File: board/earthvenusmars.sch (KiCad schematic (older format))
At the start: 33 parts, among them J1 Conn_01x05_Female, SW1 SW_SPST, SW2 SW_SPST, U1 ATSAMD21G18A-AU, U2 MIC5504-3.3YM5, Y1 32768Hz

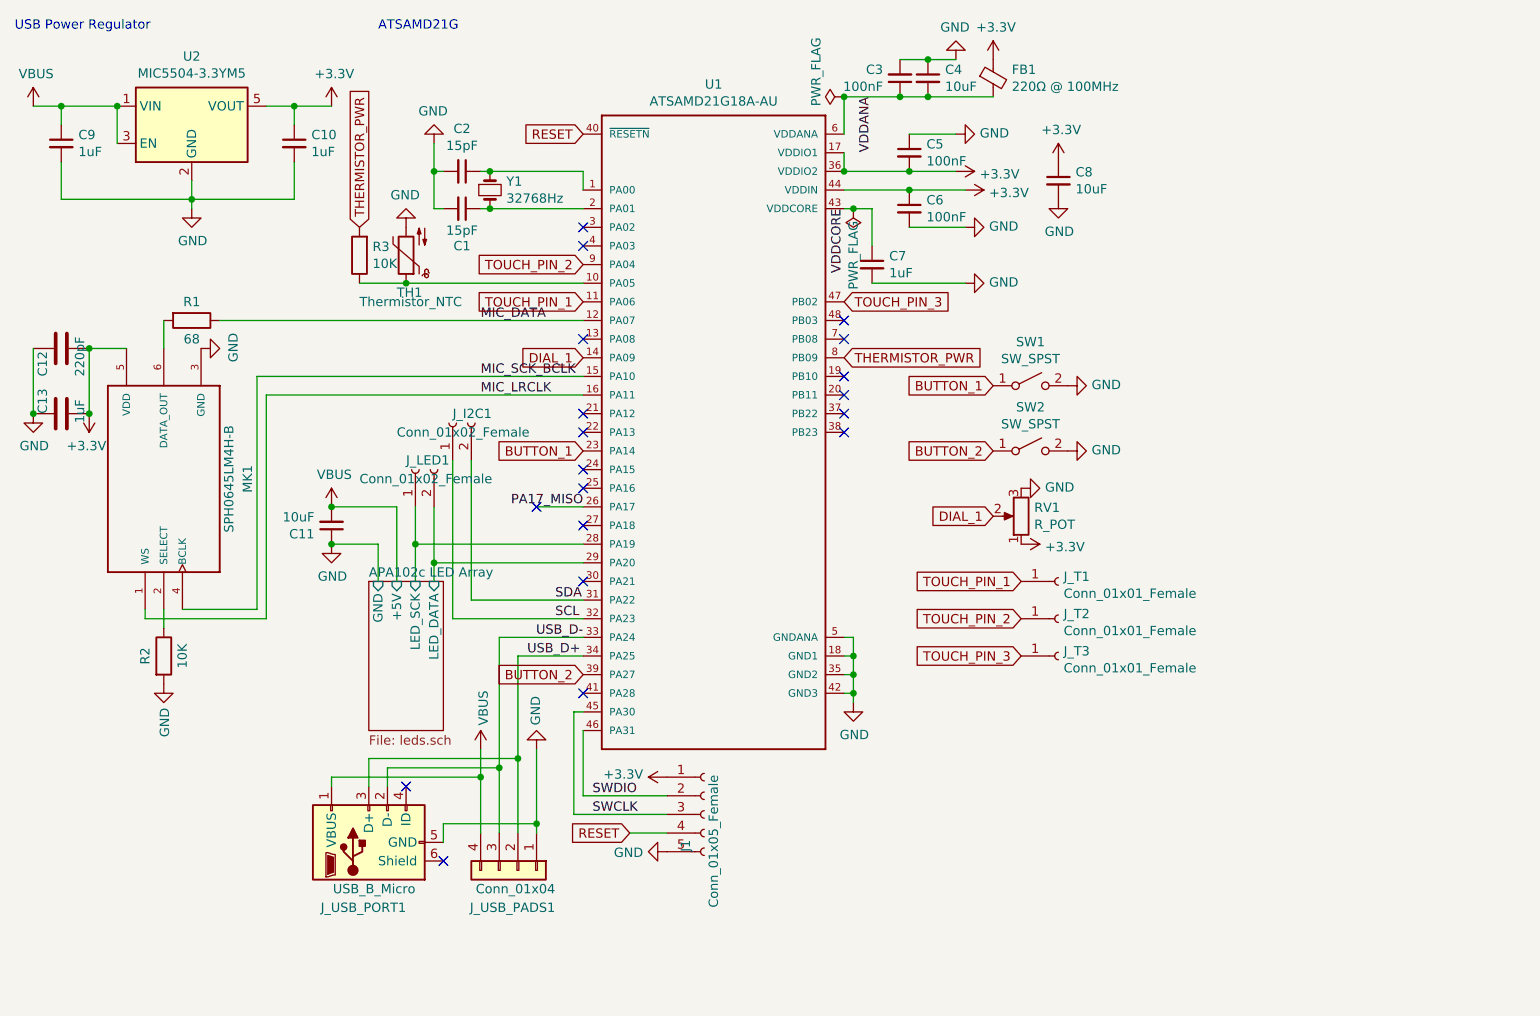
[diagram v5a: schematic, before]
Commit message: add a power switch. ugh. but it's going to prevent the device from waking up in a backpack and stuff; not to mention power draw is way too high for sleep right now
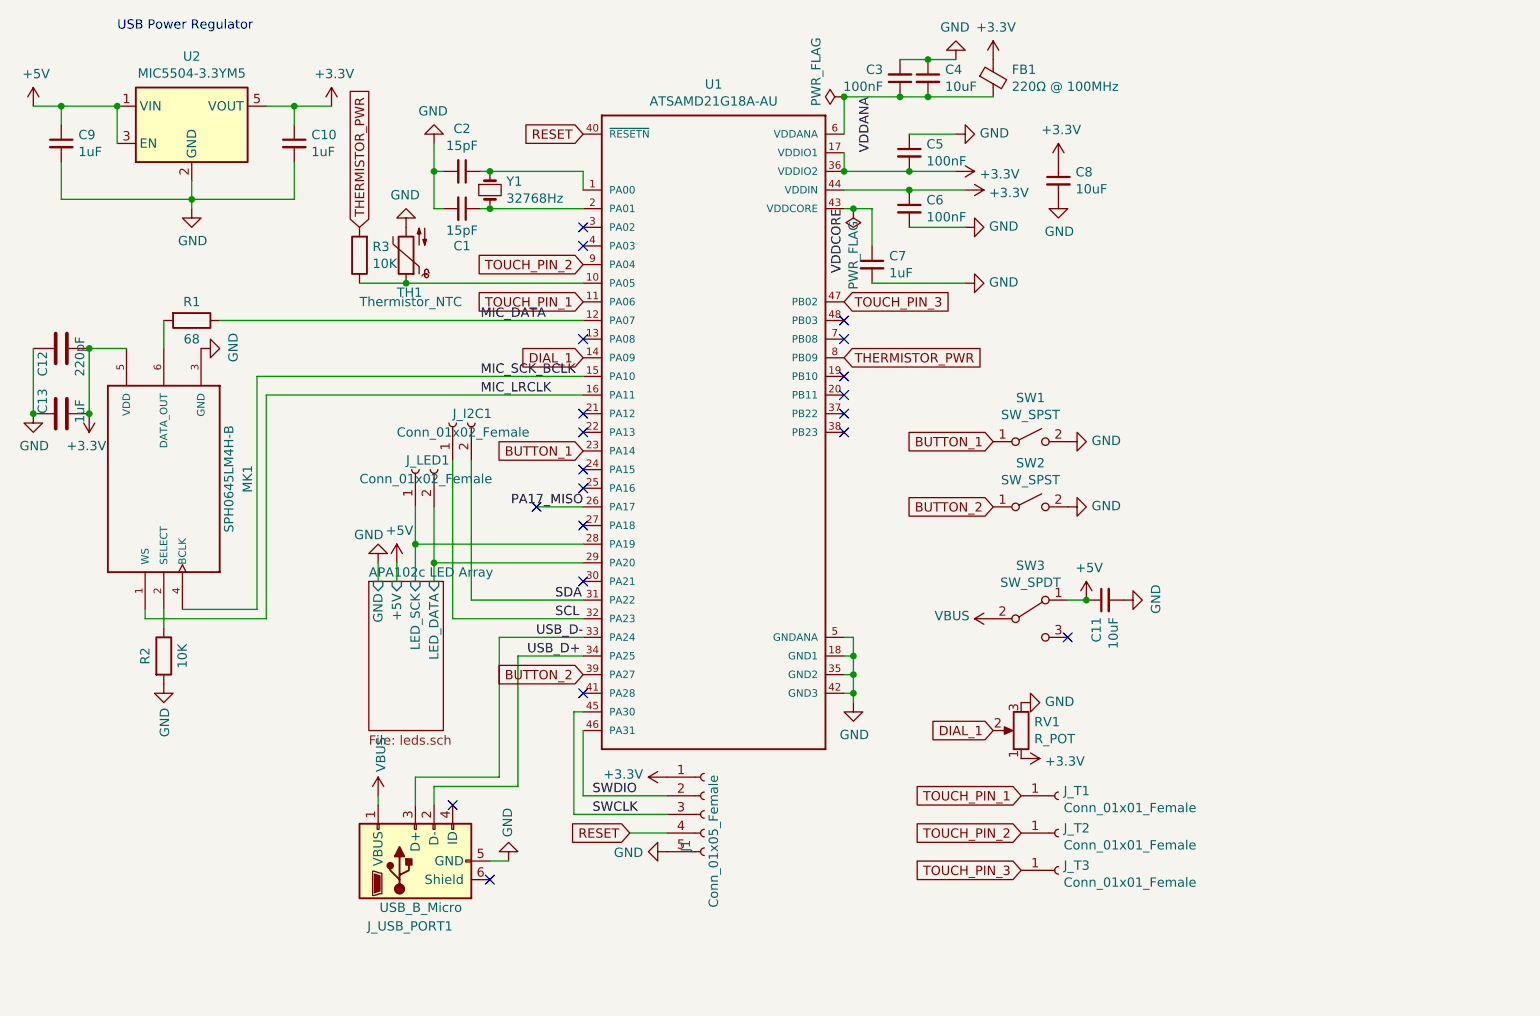
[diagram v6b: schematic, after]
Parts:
- removed J_USB_PADS1: Conn_01x04, earthvenusmars:USB_SMD, symbol Connector_Generic:Conn_01x04
- added SW3: SW_SPDT, earthvenusmars:COPAL-MFS101D-6-Z, symbol Switch:SW_SPDT
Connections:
- net GND: now also C11.2; no longer C11.1
- net USB_D+: now also J_USB_PORT1.2 (D-); no longer J_USB_PORT1.3 (D+)
- net USB_D-: now also J_USB_PORT1.3 (D+); no longer J_USB_PORT1.2 (D-)
- net VBUS: now also SW3.2 (B); no longer C11.2, C9.1, U2.1 (VIN), U2.3 (EN)
- new net +5V: C11.1, C9.1, SW3.1 (A), U2.1 (VIN), U2.3 (EN)
- no-connect marks 19 -> 20
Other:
- note removed: "ATSAMD21G"
- moved on the sheet: C11, J_T1, J_T2, J_T3, J_USB_PORT1, RV1, SW1, SW2

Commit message: clean up schematic a bit; reroute +5v to save a via
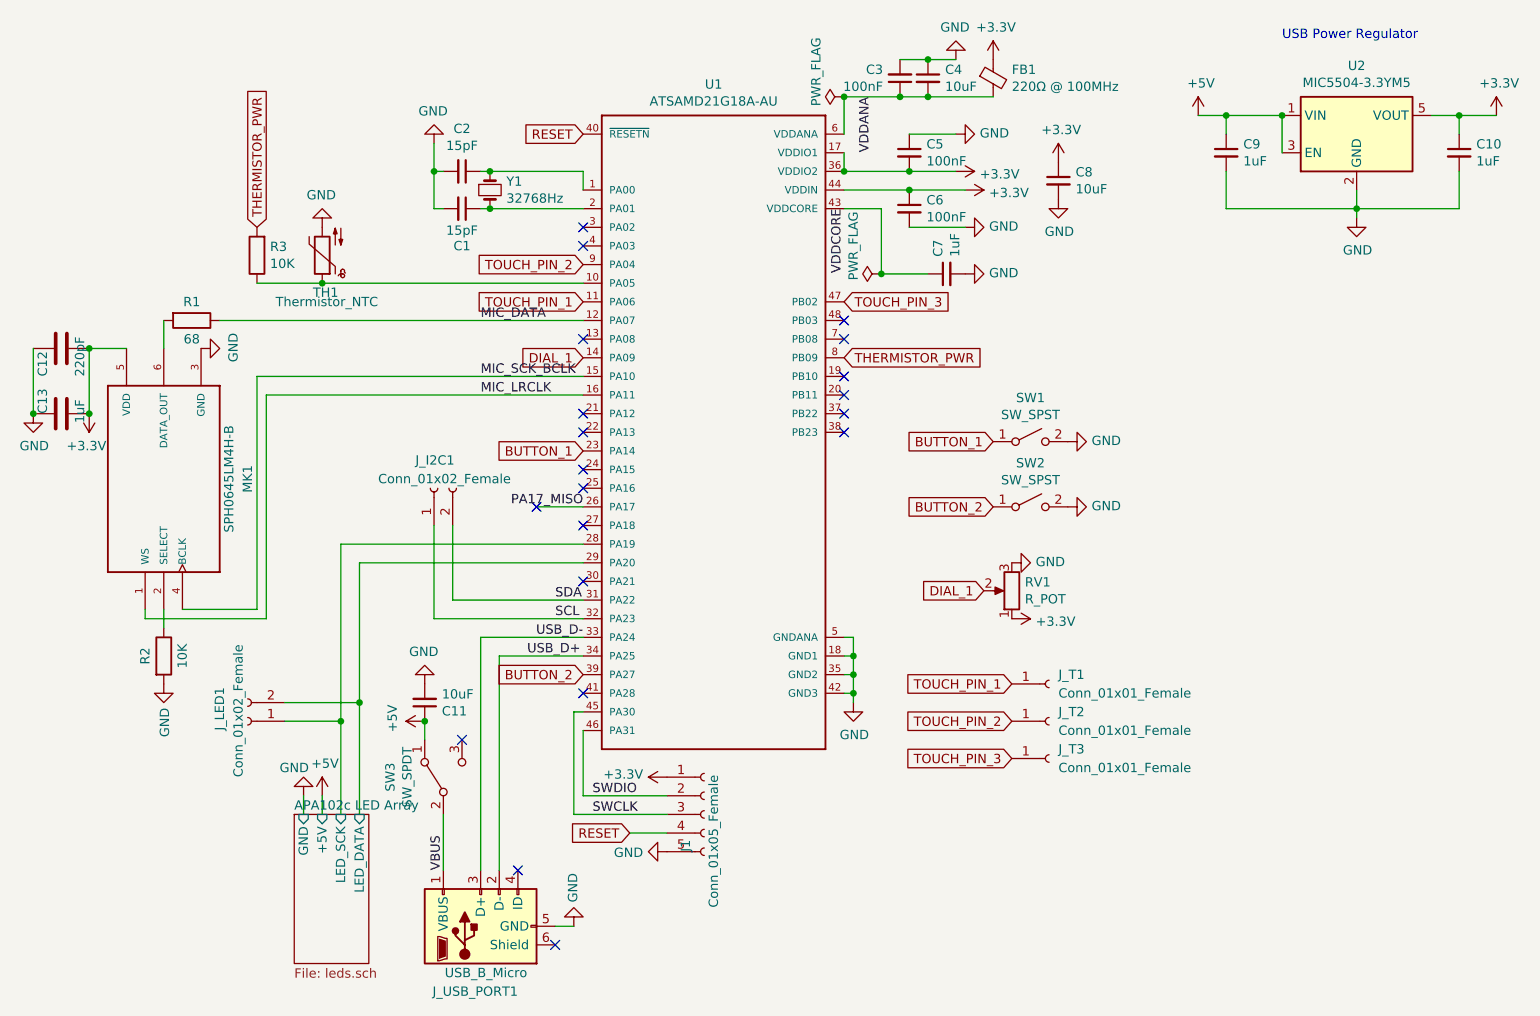
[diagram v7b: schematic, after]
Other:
- moved on the sheet: C10, C11, C7, C9, J_I2C1, J_LED1, J_T1, J_T2, J_T3, J_USB_PORT1, R3, RV1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

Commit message: add some part numbers to designation fields because fab often doesn't find the parts in other fields
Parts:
- J_USB_PORT1: Designation (none) -> USB3076-30-A
- RV1: Designation (none) -> 3352T-1-103LF
- SW3: Designation (none) -> COPAL-MFS101D-6-Z
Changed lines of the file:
@@
 F 2 "Pot_dial_3352T-1-103LF:Pot_dial_3352T-1-103LF" H 6250 3800 50  0001 C CNN
 F 3 "~" H 6250 3800 50  0001 C CNN
+F 4 "3352T-1-103LF" H 6250 3800 50  0001 C CNN "Designation"
 	1    6250 3800
 	-1   0    0    1
@@
 F 2 "earthvenusmars:COPAL-MFS101D-6-Z" H 3200 4800 50  0001 C CNN
 F 3 "~" H 3200 4800 50  0001 C CNN
+F 4 "COPAL-MFS101D-6-Z" H 3200 4800 50  0001 C CNN "Designation"
 	1    3200 4800
 	0    -1   -1   0
@@
 F 2 "Connector_USB:USB_Micro-B_GCT_USB3076-30-A" H 3550 5550 50  0001 C CNN
 F 3 "~" H 3550 5550 50  0001 C CNN
+F 4 "USB3076-30-A" H 3400 5600 50  0001 C CNN "Designation"
 	1    3400 5600
 	0    -1   -1   0
